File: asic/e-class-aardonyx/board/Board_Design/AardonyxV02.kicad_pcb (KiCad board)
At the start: 4 copper layers, 157.5 x 117.3 mm, 327 parts, among them J1 USB_B_6PIN, J10 Conn_1x6, J11 Conn_1x6, J12 Conn_1x3_M, J13 Conn_1x8_F, J14 Conn_1x6_F, J15 Conn_1x10_F, J16 Conn_1x8_F, J17 USB_OTG, J18 Conn_1x3_M, J19 Conn_1x3_M, J2 Conn_1x8, J3 Conn_1x3_M, J4 Conn_1x4, J5 PJ-202H PWRJACK, J6 Conn_1x3_M, J7 Conn_1x4, J8 Conn_1x3_M, J9 Conn_1x8, Q1 FDN339AN, SW1 SW_SPST, SW2 FSM2JSMAATR, SW3 SW_DIP_x03, U1 FT2232H, U10 TPS7A7002DDAR, U11 ADM1186, U13 TPS7A7002DDAR, U14 74AUP1G09GW, U15 SKT32E, U16 93LC56BT-I_OT, U2 IS42S32160F-TSOP2, U3 CDCE913PW, U4 TPS54627DDAR, U5 CAT24M01WI-GT3, U6 IS25LP256x-xM, U7 ADC128S102CIMTX/NOPB, U8 LSF0108PWR, U9 LSF0108PWR, Y1 12MHz, Y2 27MHz

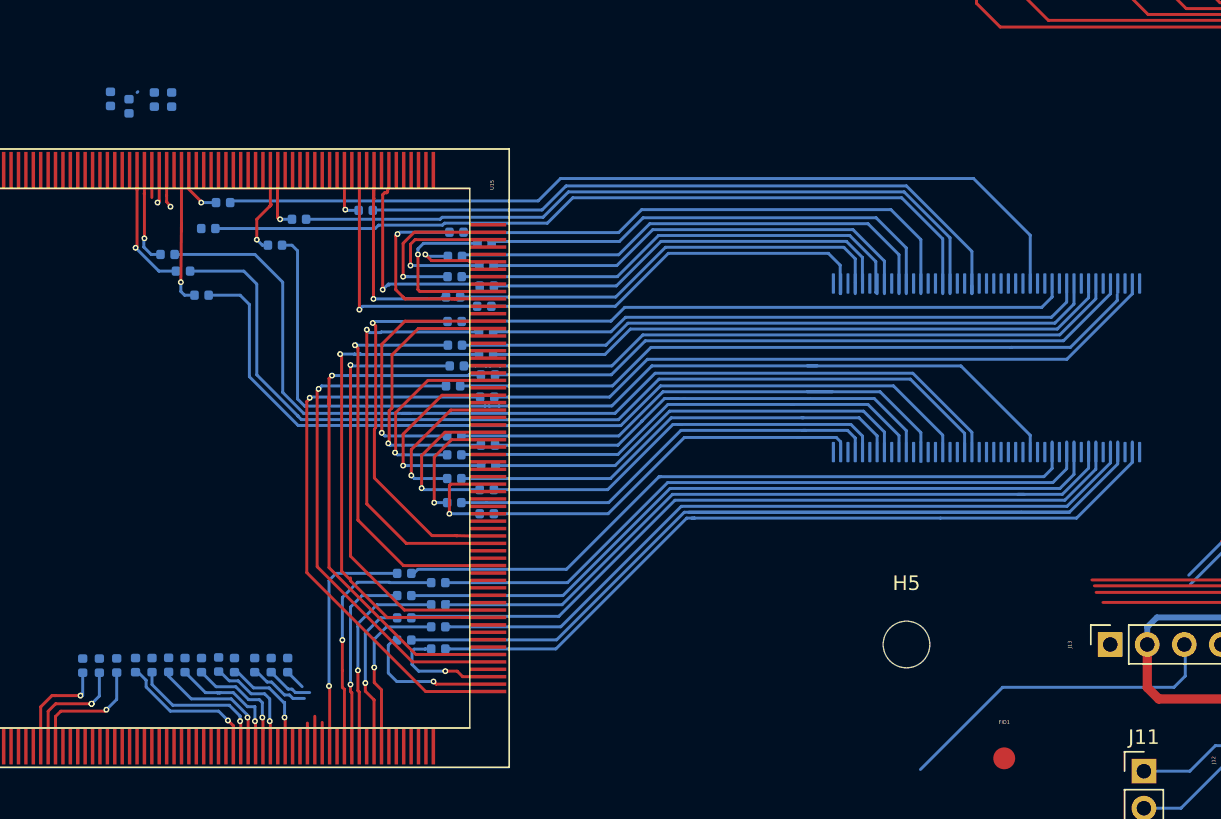
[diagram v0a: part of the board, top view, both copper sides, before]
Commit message: RAM routing update
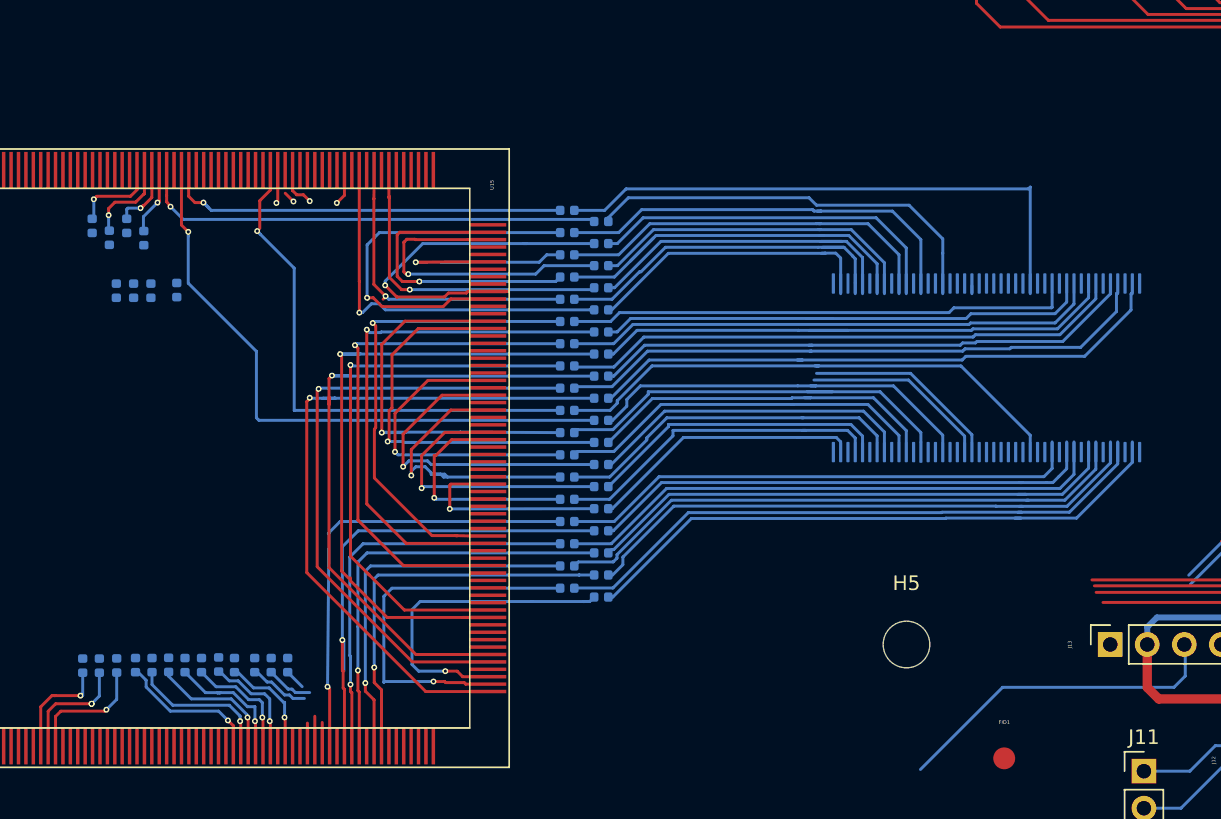
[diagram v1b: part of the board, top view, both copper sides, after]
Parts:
- moved R79 28.7 mm to (200.3, 83.9)
- moved R78 26.9 mm to (200.3, 70.3)
- moved R80 23.6 mm to (197.9, 69.5)
- moved R81 23.0 mm to (197.9, 83.2)
- moved R84 14.1 mm to (171.2, 75.0), turned to 270 degrees
- moved R87 13.5 mm to (167.0, 75.0), turned to 270 degrees
- moved R86 13.2 mm to (168.2, 75.0)
- moved R85 13.2 mm to (169.4, 75.0)
- moved R120 11.7 mm to (200.3, 96.0)
- moved R121 11.7 mm to (197.9, 95.4)
- moved R122 11.7 mm to (200.3, 94.5)
- moved R123 11.7 mm to (197.9, 93.9)
- moved R124 11.7 mm to (200.3, 93.0)
- moved R125 11.7 mm to (197.9, 92.4)
- moved R126 11.7 mm to (200.3, 91.5)
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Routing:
- net /sdram/SDRAM_CKE: track 67.7 -> 12.9 mm
- net /sdram/SDRAM_CLK: track 64.3 -> 12.3 mm
- net /sdram/SDRAM_WE: track 50.1 -> 0.00 mm
- net /sdram/SDRAM_CS: track 47.2 -> 0.55 mm
- net /sdram/SDRAM_D25: track 81.1 -> 42.5 mm
- net /sdram/SDRAM_DQM1: track 59.9 -> 26.4 mm
- net Net-(R79-Pad1): track 8.66 -> 41.1 mm
- net /sdram/SDRAM_DQM3: track 66.1 -> 35.3 mm
- net Net-(R81-Pad1): track 5.00 -> 34.6 mm
- net Net-(R78-Pad1): track 1.42 -> 30.9 mm
- net /sdram/SDRAM_DQM0: track 55.7 -> 28.7 mm
- net Net-(R80-Pad1): track 2.31 -> 26.9 mm
- net /sdram/SDRAM_DQM2: track 61.0 -> 39.2 mm
- net Net-(R126-Pad2): track 15.6 -> 32.4 mm
- net Net-(R121-Pad2): track 8.57 -> 24.2 mm
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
